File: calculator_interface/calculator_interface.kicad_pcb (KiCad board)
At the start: 2 copper layers, 146.1 x 84.1 mm, 88 parts, among them J1 Conn_02x08_Interface_Side, J2 Conn_02x20_TI30XA, J3 Conn_01x10_TI30XA, Q1 2N7000, Q10 2N7000, Q11 2N7000, Q12 2N7000, Q13 2N7000, Q14 2N7000, Q15 2N7000, Q16 2N7000, Q2 2N7000, Q3 2N7000, Q4 2N7000, Q5 2N7000, Q6 2N7000, Q7 2N7000, Q8 2N7000, Q9 2N7000, U1 MCP1700-1502E/TO, U10 LM339, U11 74HC165, U12 LM339, U13 LM339, U14 74HC595, U15 74HC595, U2 74HC165, U3 LM339, U4 LM339, U5 74HC165, U6 LM339, U7 LM339, U8 74HC165, U9 LM339

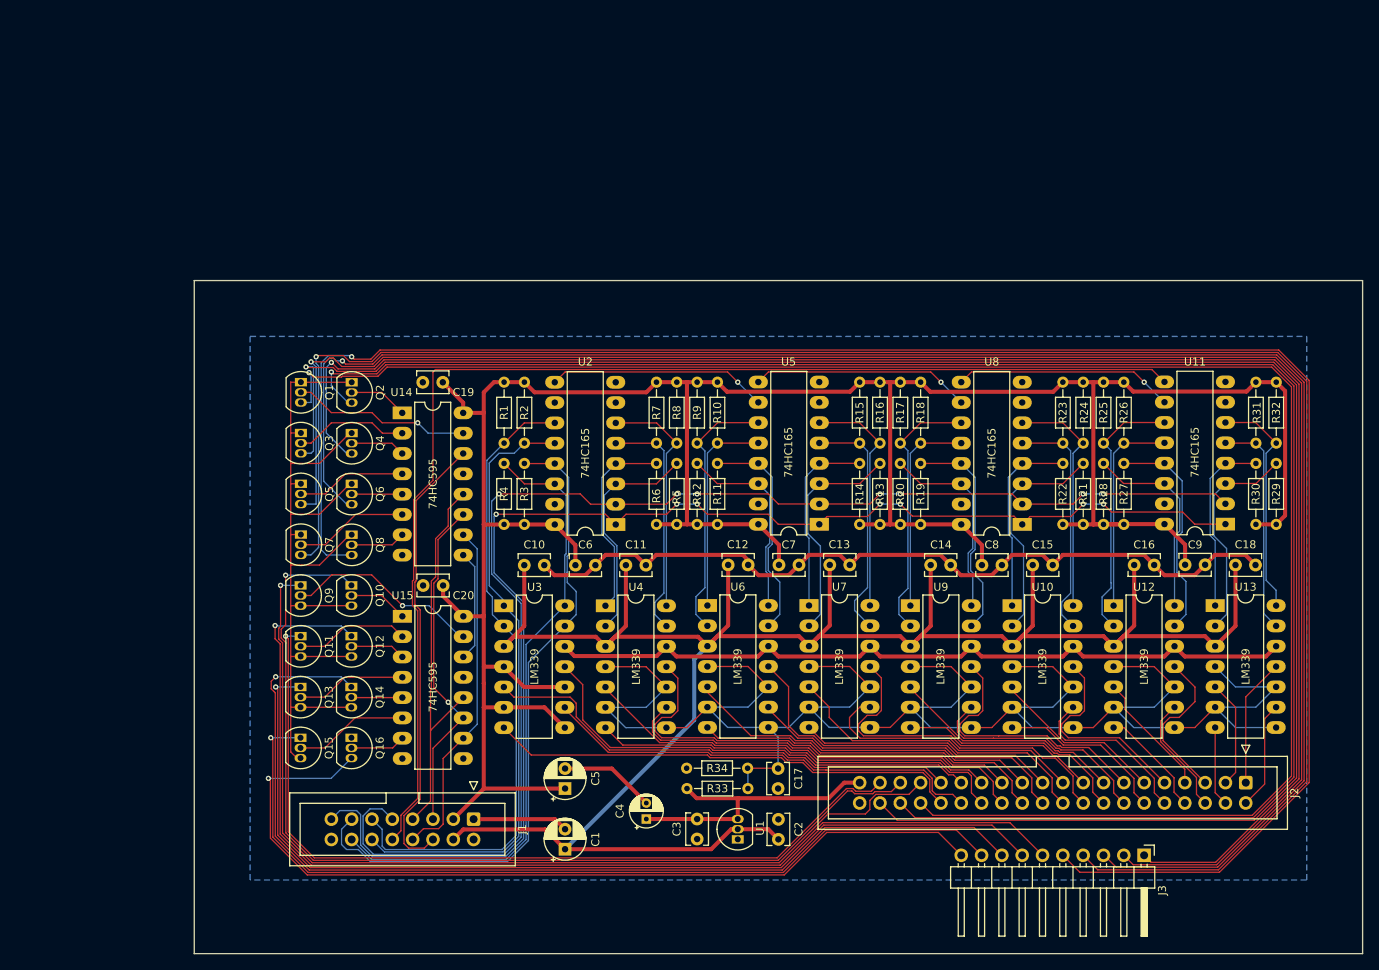
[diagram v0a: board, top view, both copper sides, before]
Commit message: add mounting holes
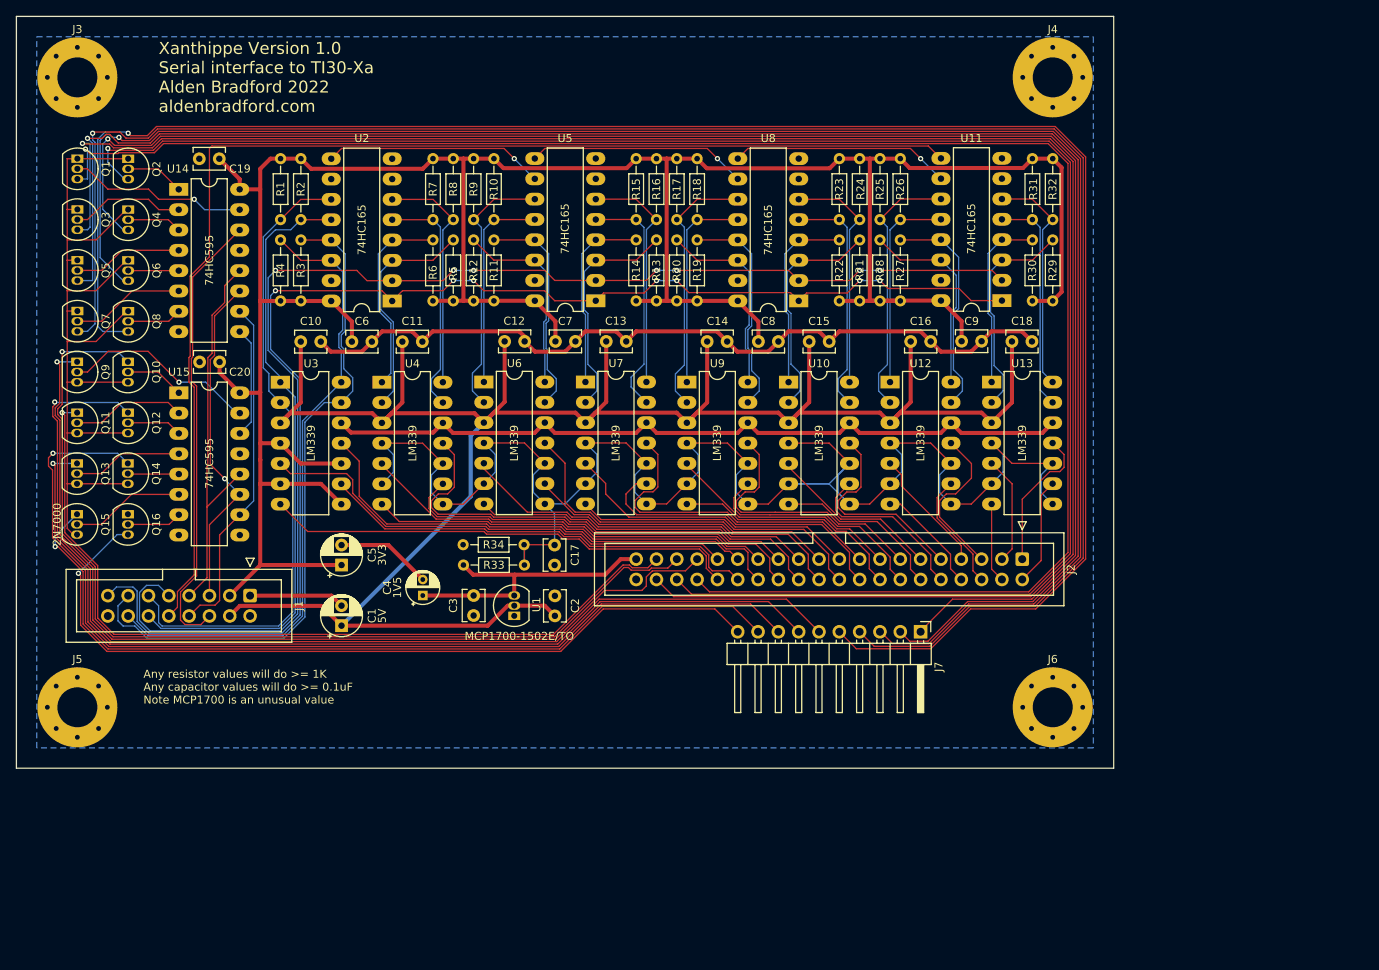
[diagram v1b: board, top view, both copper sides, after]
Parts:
- added J3: Conn_01x01, MountingHole:MountingHole_5mm_Pad_Via, F.Cu at (33.0, 33.0)
- added J4: Conn_01x01, MountingHole:MountingHole_5mm_Pad_Via, F.Cu at (154.9, 33.0)
- added J5: Conn_01x01, MountingHole:MountingHole_5mm_Pad_Via, F.Cu at (33.0, 111.8)
- added J6: Conn_01x01, MountingHole:MountingHole_5mm_Pad_Via, F.Cu at (154.9, 111.8)
- moved C2 39.5 mm to (92.7, 100.3)
- moved R26 39.5 mm to (135.9, 43.2)
- moved R27 39.5 mm to (135.9, 61.0)
- moved U6 39.5 mm to (83.8, 71.1)
- moved U9 39.5 mm to (109.2, 71.1)
- moved C19 39.5 mm to (48.3, 43.2)
- moved Q2 39.5 mm to (39.4, 43.2)
- moved Q8 39.5 mm to (39.4, 62.2)
- moved R18 39.5 mm to (110.5, 43.2)
- moved R19 39.5 mm to (110.5, 61.0)
- moved R2 39.5 mm to (61.0, 43.2)
- moved R3 39.5 mm to (61.0, 61.0)
- moved U5 39.5 mm to (97.8, 60.9)
- moved C10 39.5 mm to (60.9, 66.1)
- moved C6 39.5 mm to (69.8, 66.1)
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- renumbered J3 to J7
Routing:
- net Net-(C17-Pad1): track 230.8 -> 210.7 mm
- net /Keypad Driving/RESET: track 110.6 -> 101.7 mm
- net /Keypad Driving/B6: track 110.2 -> 105.7 mm
- net /Keypad Driving/B3: track 137.2 -> 135.2 mm
- net /LCD Reading/LCD-31: track 16.1 -> 18.0 mm
- net /Keypad Driving/B5: track 126.6 -> 124.7 mm
- net /Keypad Driving/B4: track 120.2 -> 118.4 mm
- net /Keypad Driving/B2: track 106.0 -> 104.3 mm
- net /Keypad Driving/B1: track 124.0 -> 122.3 mm
- net /LCD Reading/DAT-3: track 83.7 -> 85.2 mm
- net /Keypad Driving/B0: track 119.9 -> 118.4 mm
- net /Keypad Driving/A3: track 209.1 -> 208.3 mm
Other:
- board size 146.1 x 84.1 mm -> 137.2 x 94 mm
- board text added: "1V5"
- board text added: "2N7000"
- board text added: "3V3"
- board text added: "5V"
- board text added: "Any resistor values will do >= 1K Any capacitor values will do >= 0.1uF Note MCP1700 is an unusual value"
- board text added: "MCP1700-1502E/TO"
- board text added: "Xanthippe Version 1.0 Serial interface to TI30-Xa Alden Bradford 2022 aldenbradford.com"

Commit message: draft ready for final review
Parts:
- moved J5 2.54 mm to (33.0, 109.2)
- moved J6 2.54 mm to (154.9, 109.2)
- moved J1 0.77 mm to (54.6, 97.0)
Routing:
- net Net-(C17-Pad1): track 210.7 -> 197.1 mm
- net +5V: track 262.4 -> 258.5 mm
- net GND: track 221.0 -> 223.8 mm
- net /LCD Reading/LCD-16: track 38.7 -> 37.1 mm
- net /Keypad Driving/DATA: track 56.7 -> 55.9 mm
- net /LCD Reading/DATA: track 153.3 -> 152.5 mm
- net /Keypad Driving/CLOCK: track 42.7 -> 41.9 mm
- net /LCD Reading/DAT-1: track 80.4 -> 79.7 mm
- net /Keypad Driving/~{BLANK}: track 43.3 -> 42.6 mm
- net /LCD Reading/LCD-13: track 37.5 -> 36.8 mm
- net /LCD Reading/CLOCK: track 168.6 -> 167.9 mm
- net /Keypad Driving/SHOW: track 49.0 -> 48.4 mm
- net /LCD Reading/~{SAMPLE}: track 170.0 -> 169.4 mm
- net /LCD Reading/DAT-3: track 85.2 -> 84.7 mm
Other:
- board size 137.2 x 94 mm -> 137.2 x 91.4 mm
- rule pad_to_mask_clearance: 0.000051 -> 0
- board text added: "JLCJLCJLCJLC"

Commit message: changed reference voltage circuit to be compatible with voltage regulator
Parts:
- R33, R34: value 100K -> 100R; footprint Resistor_THT:R_Axial_DIN0204_L3.6mm_D1.6mm_P7.62mm_Horizontal -> Resistor_THT:R_Axial_DIN0207_L6.3mm_D2.5mm_P10.16mm_Horizontal
- moved R33 2.59 mm to (78.7, 94.5)
- moved C4 1.27 mm to (74.9, 97.8)
- moved C17 0.98 mm to (91.7, 91.4)
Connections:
- net Net-(C17-Pad1) renamed /LCD Reading/Comparator reference
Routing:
- net GND: track 223.8 -> 244.4 mm
- net /LCD Reading/Comparator reference: track 197.1 -> 200.3 mm
- net +1V5: track 36.4 -> 34.5 mm
- net +5V: track 258.5 -> 257.8 mm
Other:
- board text removed: "Any resistor values will do >= 1K Any capacitor values will do >= 0.1uF Note MCP1700 is an unusual value"
